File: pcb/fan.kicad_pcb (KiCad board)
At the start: 2 copper layers, 290.9 x 267.8 mm, 196 parts, among them J2 Pi, SW1 SW_PUSH, SW10 SW_PUSH, SW11 SW_PUSH, SW12 SW_PUSH, SW13 SW_PUSH, SW14 SW_PUSH, SW15 SW_PUSH, SW16 SW_PUSH, SW17 SW_PUSH, SW18 SW_PUSH, SW19 SW_PUSH, SW2 SW_PUSH, SW20 SW_PUSH, SW21 SW_PUSH, SW22 SW_PUSH, SW23 SW_PUSH, SW24 SW_PUSH, SW25 SW_PUSH, SW26 SW_PUSH, SW27 SW_PUSH, SW28 SW_PUSH, SW29 SW_PUSH, SW3 SW_PUSH, SW30 SW_PUSH, SW31 SW_PUSH, SW32 SW_PUSH, SW33 SW_PUSH, SW34 SW_PUSH, SW35 SW_PUSH, SW36 SW_PUSH, SW37 SW_PUSH, SW38 SW_PUSH, SW39 SW_PUSH, SW4 SW_PUSH, SW40 SW_PUSH, SW41 SW_PUSH, SW42 SW_PUSH, SW43 SW_PUSH, SW44 SW_PUSH, SW45 SW_PUSH, SW46 SW_PUSH, SW47 SW_PUSH, SW48 SW_PUSH, SW49 SW_PUSH, SW5 SW_PUSH, SW50 SW_PUSH, SW51 SW_PUSH, SW52 SW_PUSH, SW53 SW_PUSH, SW54 SW_PUSH, SW55 SW_PUSH, SW56 SW_PUSH, SW57 SW_PUSH, SW58 SW_PUSH, SW59 SW_PUSH, SW6 SW_PUSH, SW60 SW_PUSH, SW61 SW_PUSH, SW62 SW_PUSH, SW63 SW_PUSH, SW64 SW_PUSH, SW65 SW_PUSH, SW66 SW_PUSH, SW67 SW_PUSH, SW68 SW_PUSH, SW69 SW_PUSH, SW7 SW_PUSH, SW70 SW_PUSH, SW71 SW_PUSH, SW72 SW_PUSH, SW73 SW_PUSH, SW74 SW_PUSH, SW75 SW_PUSH, SW76 SW_PUSH, SW77 SW_PUSH, SW78 SW_PUSH, SW79 SW_PUSH, SW8 SW_PUSH, SW80 SW_PUSH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

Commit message: v2.0 外形考え中
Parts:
- removed D1, D10, D11, D12, D13, D14, D15, D16, D17, D18, D19, D2, D20, D21, D22, D23, D24, D25, D26, D27, D28, D29, D3, D30, D31, D32, D33, D34, D35, D36, D37, D38, D39, D4, D40, D41, D42, D43, D44, D45, D46, D47, D48, D49, D5, D50, D51, D52, D53, D54, D55, D56, D57, D58, D59, D6, D60, D61, D62, D63, D64, D65, D66, D67, D68, D69, D7, D70, D71, D72, D73, D74, D75, D76, D77, D78, D79, D8, D80, D81, D82, D83, D84, D85, D86, D87, D88, D89, D9, D90: DIODE, kbd:D3_TH_SMD
- removed HOLE1, HOLE2, HOLE3, HOLE4, HOLE5, HOLE6: Val**, kbd:HOLE
- removed J2: Pi, kbd:PinSocket_2x20_P2.54mm_Vertical_edit_wakunasi
- removed SW43, SW44, SW45, SW46, SW47, SW48, SW51, SW52, SW53, SW54, SW56, SW57, SW58, SW59, SW60, SW61, SW62, SW63, SW64, SW65, SW66, SW67, SW68, SW69, SW70, SW71, SW72, SW73, SW74, SW75, SW76, SW77, SW78, SW79, SW80, SW81, SW82, SW83, SW84, SW85, SW86, SW87, SW88, SW89, SW90: SW_PUSH, kbd:CherryMX_Hotswap_edit_wakunasi
- removed SW49, SW50, SW55, SW91, SW92: SW_PUSH, kbd:ResetSW_wakunasi
- removed SW93: SW_SPDT, kbd:SW_Slide_edit_wakunasi
- removed U4, U6: 74HC595, kbd:SN74HC595_DIP-16_W7.62mm_Socket_2
- added J*: MJ-4PP-9, kbd:MJ-4PP-9, F.Cu at (197.3, 19.1)
- SW1, SW11, SW12, SW13, SW14, SW16, SW17, SW18, SW19, SW2, SW20, SW21, SW22, SW23, SW24, SW25, SW26, SW27, SW28, SW29, SW3, SW30, SW31, SW32, SW33, SW34, SW35, SW36, SW37, SW38, SW39, SW4, SW40, SW6, SW7, SW8, SW9: value SW_PUSH -> SW_PUSH-kbd; footprint kbd:CherryMX_Hotswap_edit_wakunasi -> kbd:CherryMX_MidHeight_Hotswap_edit
- SW10, SW15, SW5: value SW_PUSH -> SW_PUSH-kbd; footprint kbd:CherryMX_Hotswap_edit_wakunasi -> kbd:ResetSW_with_diode
- SW41, SW42: footprint kbd:CherryMX_Hotswap_edit_wakunasi -> kbd:ResetSW
- moved SW36 130.0 mm to (159.4, 32.0), turned to 352 degrees
- moved SW6 125.4 mm to (41.3, 46.1), turned to 26 degrees
- moved SW11 108.9 mm to (60.3, 38.4)
- moved SW42 108.6 mm to (190.8, 72.9), turned to 90 degrees
- moved SW12 105.5 mm to (58.2, 59.6), turned to 22 degrees
- moved SW41 90.4 mm to (190.8, 62.6), turned to 90 degrees
- moved SW17 87.7 mm to (78.0, 53.8), turned to 13 degrees
- moved SW16 87.3 mm to (80.2, 33.4), turned to 10 degrees
- moved SW18 86.8 mm to (81.7, 72.6), turned to 13 degrees
- moved SW5 75.9 mm to (91.0, 103.0), turned to 194 degrees
- moved U2 73.3 mm to (183.2, 41.2), turned to 180 degrees
- moved U1 71.4 mm to (180.6, 40.1), turned to 0 degrees
- moved SW23 68.2 mm to (101.1, 69.0), turned to 8 degrees
- moved SW22 65.8 mm to (97.7, 50.3), turned to 8 degrees
- moved SW21 65.5 mm to (99.7, 30.3), turned to 6 degrees
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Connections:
- SW1 pad 1: (no net) -> col00
- SW1 pad 2: (no net) -> Net-(SW1-Pad2)
- SW10 pad 1: (no net) -> col01
- SW10 pad 2: (no net) -> Net-(SW10-Pad2)
- SW11 pad 1: (no net) -> col02
- SW11 pad 2: (no net) -> Net-(SW11-Pad2)
- SW12 pad 1: (no net) -> col02
- SW12 pad 2: (no net) -> Net-(SW12-Pad2)
- SW13 pad 1: (no net) -> col02
- SW13 pad 2: (no net) -> Net-(SW13-Pad2)
- SW14 pad 1: (no net) -> col02
- SW14 pad 2: (no net) -> Net-(SW14-Pad2)
- SW15 pad 1: (no net) -> col02
- SW15 pad 2: (no net) -> Net-(SW15-Pad2)
- SW16 pad 1: (no net) -> col03
- SW16 pad 2: (no net) -> Net-(SW16-Pad2)
- SW17 pad 1: (no net) -> col03
- SW17 pad 2: (no net) -> Net-(SW17-Pad2)
- SW18 pad 1: (no net) -> col03
- SW18 pad 2: (no net) -> Net-(SW18-Pad2)
- SW19 pad 1: (no net) -> col03
- SW19 pad 2: (no net) -> Net-(SW19-Pad2)
- SW2 pad 1: (no net) -> col00
- SW2 pad 2: (no net) -> Net-(SW2-Pad2)
- SW20 pad 1: (no net) -> col03
- SW20 pad 2: (no net) -> Net-(SW20-Pad2)
- SW21 pad 1: (no net) -> col04
- SW21 pad 2: (no net) -> Net-(SW21-Pad2)
- SW22 pad 1: (no net) -> col04
- SW22 pad 2: (no net) -> Net-(SW22-Pad2)
- SW23 pad 1: (no net) -> col04
- SW23 pad 2: (no net) -> Net-(SW23-Pad2)
- SW24 pad 1: (no net) -> col04
- SW24 pad 2: (no net) -> Net-(SW24-Pad2)
- SW25 pad 1: (no net) -> col04
- SW25 pad 2: (no net) -> Net-(SW25-Pad2)
- SW26 pad 1: (no net) -> col05
- SW26 pad 2: (no net) -> Net-(SW26-Pad2)
- SW27 pad 1: (no net) -> col05
- SW27 pad 2: (no net) -> Net-(SW27-Pad2)
- SW28 pad 1: (no net) -> col05
- SW28 pad 2: (no net) -> Net-(SW28-Pad2)
- SW29 pad 1: (no net) -> col05
- SW29 pad 2: (no net) -> Net-(SW29-Pad2)
- SW3 pad 1: (no net) -> col00
- SW3 pad 2: (no net) -> Net-(SW3-Pad2)
- SW30 pad 1: (no net) -> col05
- SW30 pad 2: (no net) -> Net-(SW30-Pad2)
- SW31 pad 1: (no net) -> col06
- SW31 pad 2: (no net) -> Net-(SW31-Pad2)
- SW32 pad 1: (no net) -> col06
- SW32 pad 2: (no net) -> Net-(SW32-Pad2)
- SW33 pad 1: (no net) -> col06
- SW33 pad 2: (no net) -> Net-(SW33-Pad2)
- SW34 pad 1: (no net) -> col06
- SW34 pad 2: (no net) -> Net-(SW34-Pad2)
- SW35 pad 1: (no net) -> col06
- SW35 pad 2: (no net) -> Net-(SW35-Pad2)
- SW36 pad 1: (no net) -> col07
- SW36 pad 2: (no net) -> Net-(SW36-Pad2)
- SW37 pad 1: (no net) -> col07
- SW37 pad 2: (no net) -> Net-(SW37-Pad2)
- SW38 pad 1: (no net) -> col07
- SW38 pad 2: (no net) -> Net-(SW38-Pad2)
- SW39 pad 1: (no net) -> col07
- SW39 pad 2: (no net) -> Net-(SW39-Pad2)
- SW4 pad 1: (no net) -> col00
- SW4 pad 2: (no net) -> Net-(SW4-Pad2)
- SW40 pad 1: (no net) -> col07
- SW40 pad 2: (no net) -> Net-(SW40-Pad2)
- SW41 pad 1: (no net) -> software_reset
- SW41 pad 2: (no net) -> GND
- SW42 pad 1: (no net) -> hardware_reset
- SW42 pad 2: (no net) -> GND
- SW5 pad 1: (no net) -> col00
- SW5 pad 2: (no net) -> Net-(SW5-Pad2)
- SW6 pad 1: (no net) -> col01
- SW6 pad 2: (no net) -> Net-(SW6-Pad2)
- SW7 pad 1: (no net) -> col01
- SW7 pad 2: (no net) -> Net-(SW7-Pad2)
- SW8 pad 1: (no net) -> col01
- SW8 pad 2: (no net) -> Net-(SW8-Pad2)
- SW9 pad 1: (no net) -> col01
- SW9 pad 2: (no net) -> Net-(SW9-Pad2)
- U1 pad 10: (no net) -> SCL
- U1 pad 11: (no net) -> RCK
- U1 pad 12: (no net) -> OE
- U1 pad 14: (no net) -> row04
- U1 pad 15: (no net) -> row03
- U1 pad 16: (no net) -> row02
- U1 pad 17: (no net) -> row01
- U1 pad 18: (no net) -> row00
- U1 pad 21: (no net) -> VCC
- U1 pad 22: (no net) -> hardware_reset
- U1 pad 23: (no net) -> GND
- U1 pad 3: (no net) -> GND
- U1 pad 4: (no net) -> GND
- U1 pad 7: (no net) -> software_reset
- U1 pad 8: (no net) -> SER
- U1 pad 9: (no net) -> SCK
- U2 pad 10: (no net) -> SCL
- U2 pad 11: (no net) -> RCK
- U2 pad 12: (no net) -> OE
- U2 pad 14: (no net) -> row04
- U2 pad 15: (no net) -> row03
- U2 pad 16: (no net) -> row02
- U2 pad 17: (no net) -> row01
- U2 pad 18: (no net) -> row00
- U2 pad 21: (no net) -> VCC
- U2 pad 22: (no net) -> hardware_reset
- U2 pad 23: (no net) -> GND
- U2 pad 3: (no net) -> GND
- U2 pad 4: (no net) -> GND
- U2 pad 7: (no net) -> software_reset
- U2 pad 8: (no net) -> SER
- U2 pad 9: (no net) -> SCK
- U3 pad 1: (no net) -> col01
- U3 pad 10: (no net) -> SCL
- U3 pad 11: (no net) -> SCK
- U3 pad 12: (no net) -> RCK
- U3 pad 13: (no net) -> OE
- U3 pad 14: (no net) -> SER
- U3 pad 15: (no net) -> col00
- U3 pad 16: (no net) -> VCC
- U3 pad 2: (no net) -> col02
- U3 pad 3: (no net) -> col03
- U3 pad 4: (no net) -> col04
- U3 pad 5: (no net) -> col05
- U3 pad 6: (no net) -> col06
- U3 pad 7: (no net) -> col07
- U3 pad 8: (no net) -> GND
- U5 pad 1: (no net) -> col01
- U5 pad 10: (no net) -> SCL
- U5 pad 11: (no net) -> SCK
- U5 pad 12: (no net) -> RCK
- U5 pad 13: (no net) -> OE
- U5 pad 14: (no net) -> SER
- U5 pad 15: (no net) -> col00
- U5 pad 16: (no net) -> VCC
- U5 pad 2: (no net) -> col02
- U5 pad 3: (no net) -> col03
- U5 pad 4: (no net) -> col04
- U5 pad 5: (no net) -> col05
- U5 pad 6: (no net) -> col06
- U5 pad 7: (no net) -> col07
- U5 pad 8: (no net) -> GND
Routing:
- net (no net): track 11725.6 -> 0.00 mm, vias 448 -> 0
- net col00: track 0.00 -> 384.7 mm
- net col01: track 0.00 -> 360.8 mm
- net col02: track 0.00 -> 326.7 mm, vias 0 -> 1
- net col03: track 0.00 -> 326.6 mm
- net col04: track 0.00 -> 314.3 mm, vias 0 -> 1
- net col07: track 0.00 -> 301.8 mm, vias 0 -> 1
- net col05: track 0.00 -> 297.4 mm, vias 0 -> 2
- net col06: track 0.00 -> 296.7 mm, vias 0 -> 3
- net row04: track 0.00 -> 257.3 mm
- net row03: track 0.00 -> 238.2 mm
- net row00: track 0.00 -> 219.1 mm
- net row02: track 0.00 -> 218.9 mm
- net row01: track 0.00 -> 208.6 mm
- net hardware_reset: track 0.00 -> 58.6 mm
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- added copper zone on B.Cu, net GND
- added copper zone on F.Cu, net GND
- removed copper zone on B.Cu, net (none)
- removed copper zone on F.Cu, net (none)
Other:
- board size 290.9 x 267.8 mm -> 211.6 x 146.1 mm

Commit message: 迷走中...元にもどす
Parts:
- moved U1 141.3 mm to (52.7, 100.2), turned to 39 degrees
- moved U2 140.4 mm to (55.4, 99.4), turned to 219 degrees
- moved SW42 127.8 mm to (63.1, 76.3), turned to 215 degrees
- moved SW41 125.6 mm to (66.7, 81.5), turned to 215 degrees
- moved U3 124.8 mm to (66.6, 124.1), turned to 41 degrees
- moved U5 123.6 mm to (69.6, 123.3), turned to 221 degrees
- moved SW15 57.3 mm to (167.6, 111.8)
- moved SW16 57.3 mm to (136.2, 45.6)
- moved SW19 57.3 mm to (131.6, 107.1)
- moved SW1 57.3 mm to (79.6, 68.8)
- moved SW10 57.3 mm to (157.2, 113.1)
- moved SW11 57.3 mm to (116.3, 50.6)
- moved SW12 57.3 mm to (114.2, 71.8)
- moved SW17 57.3 mm to (134.1, 66.0)
- moved SW21 57.3 mm to (155.8, 42.5)
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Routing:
- net col00: track 384.7 -> 202.3 mm
- net col01: track 360.8 -> 196.3 mm
- net col02: track 326.7 -> 199.0 mm
- net col04: track 314.3 -> 230.0 mm
- net col07: track 301.8 -> 219.8 mm
- net row04: track 257.3 -> 181.5 mm
- net col05: track 297.4 -> 224.8 mm, vias 2 -> 0
- net hardware_reset: track 58.6 -> 0.00 mm
- net row03: track 238.2 -> 181.2 mm
- net row02: track 218.9 -> 163.5 mm
- net VCC: track 54.6 -> 0.00 mm
- net SCL: track 48.5 -> 0.00 mm
- net SCK: track 48.5 -> 0.00 mm
- net SER: track 41.5 -> 0.00 mm
- net RCK: track 38.2 -> 0.00 mm
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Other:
- board size 211.6 x 146.1 mm -> 590.2 x 634.1 mm

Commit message: 基盤の外形を決定した
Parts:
- removed J*: MJ-4PP-9, kbd:MJ-4PP-9
- added J1: MJ-4PP-9, kbd:MJ-4PP-9, F.Cu at (228.4, 74.5)
- added Ref**: Val**, kbd:HOLE, F.Cu at (42.6, 68.3)
- added Ref**: Val**, kbd:HOLE, F.Cu at (198.7, 26.1)
- added Ref**: Val**, kbd:HOLE, F.Cu at (137.4, 105.4)
- added Ref**: Val**, kbd:HOLE, F.Cu at (232.1, 125.2)
- added Ref**: Val**, kbd:HOLE, F.Cu at (48.8, 115.2)
- moved U1 162.7 mm to (206.1, 46.0), turned to 0 degrees
- moved U2 161.9 mm to (208.7, 47.3), turned to 180 degrees
- moved SW41 158.7 mm to (225.4, 83.2), turned to 90 degrees
- moved SW42 155.0 mm to (218.0, 83.2), turned to 90 degrees
- moved U3 145.7 mm to (203.2, 73.3), turned to 0 degrees
- moved U5 144.8 mm to (206.0, 74.7), turned to 180 degrees
- moved SW10 33.5 mm to (126.5, 99.8)
- moved SW15 33.5 mm to (136.9, 98.5)
- moved SW16 33.5 mm to (105.5, 32.3)
- moved SW17 33.5 mm to (103.4, 52.7)
- moved SW19 33.5 mm to (100.9, 93.8)
- moved SW25 33.5 mm to (173.7, 108.1)
- moved SW26 33.5 mm to (145.1, 28.0)
- moved SW27 33.5 mm to (143.2, 47.2)
- moved SW28 33.5 mm to (146.5, 66.5)
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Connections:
- U1 pad 10: SCL -> RCK
- U1 pad 11: RCK -> OE
- U1 pad 12: OE -> SER
- U1 pad 2: (no net) -> data
- U1 pad 8: SER -> SCL
- U2 pad 10: SCL -> RCK
- U2 pad 11: RCK -> OE
- U2 pad 12: OE -> SER
- U2 pad 2: (no net) -> data
- U2 pad 8: SER -> SCL
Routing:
- net col00: track 202.3 -> 394.1 mm
- net col01: track 196.3 -> 365.6 mm
- net col02: track 199.0 -> 332.7 mm
- net col04: track 230.0 -> 321.1 mm
- net col07: track 219.8 -> 309.0 mm
- net VCC: track 0.00 -> 75.9 mm
- net row04: track 181.5 -> 250.2 mm
- net hardware_reset: track 0.00 -> 67.0 mm
- net software_reset: track 0.00 -> 64.3 mm
- net data: track 0.00 -> 62.0 mm
- net SCL: track 0.00 -> 60.3 mm
- net SCK: track 0.00 -> 54.6 mm
- net col05: track 224.8 -> 279.1 mm, vias 0 -> 1
- net col03: track 288.5 -> 341.3 mm, vias 0 -> 1
- net row03: track 181.2 -> 231.0 mm
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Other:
- board size 590.2 x 634.1 mm -> 211.3 x 140.3 mm

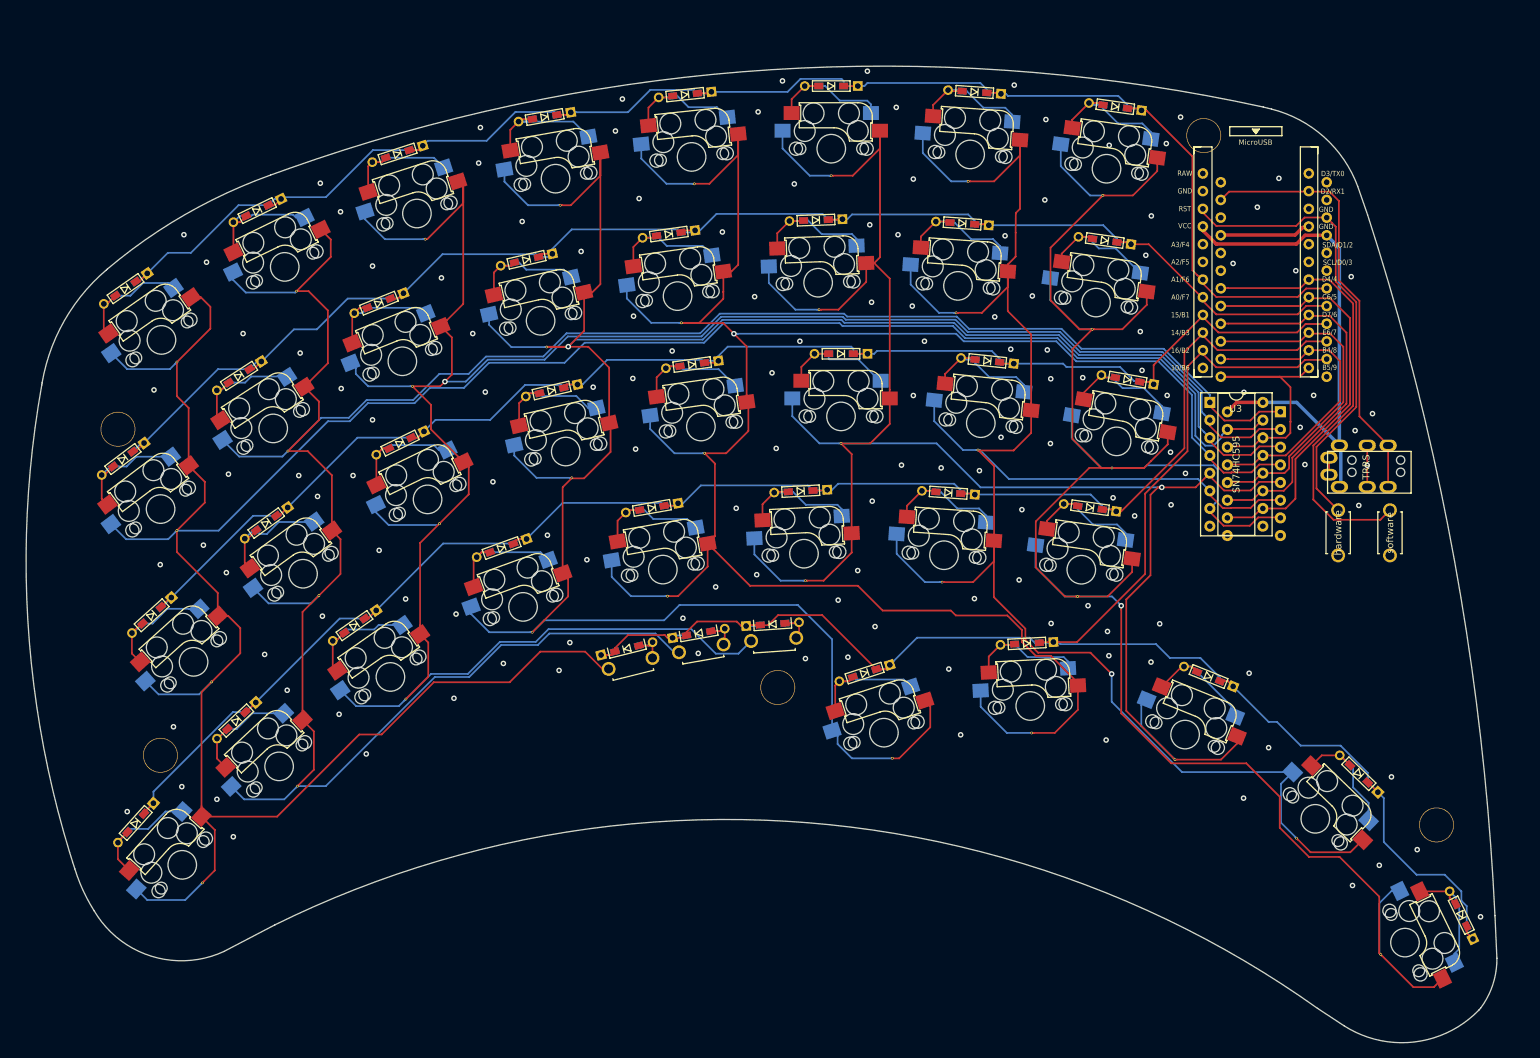
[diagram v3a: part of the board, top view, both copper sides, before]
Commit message: v2.0 fan90を受けて修正。これでpro micro用の回路は官僚とする。(ケースはまだない)
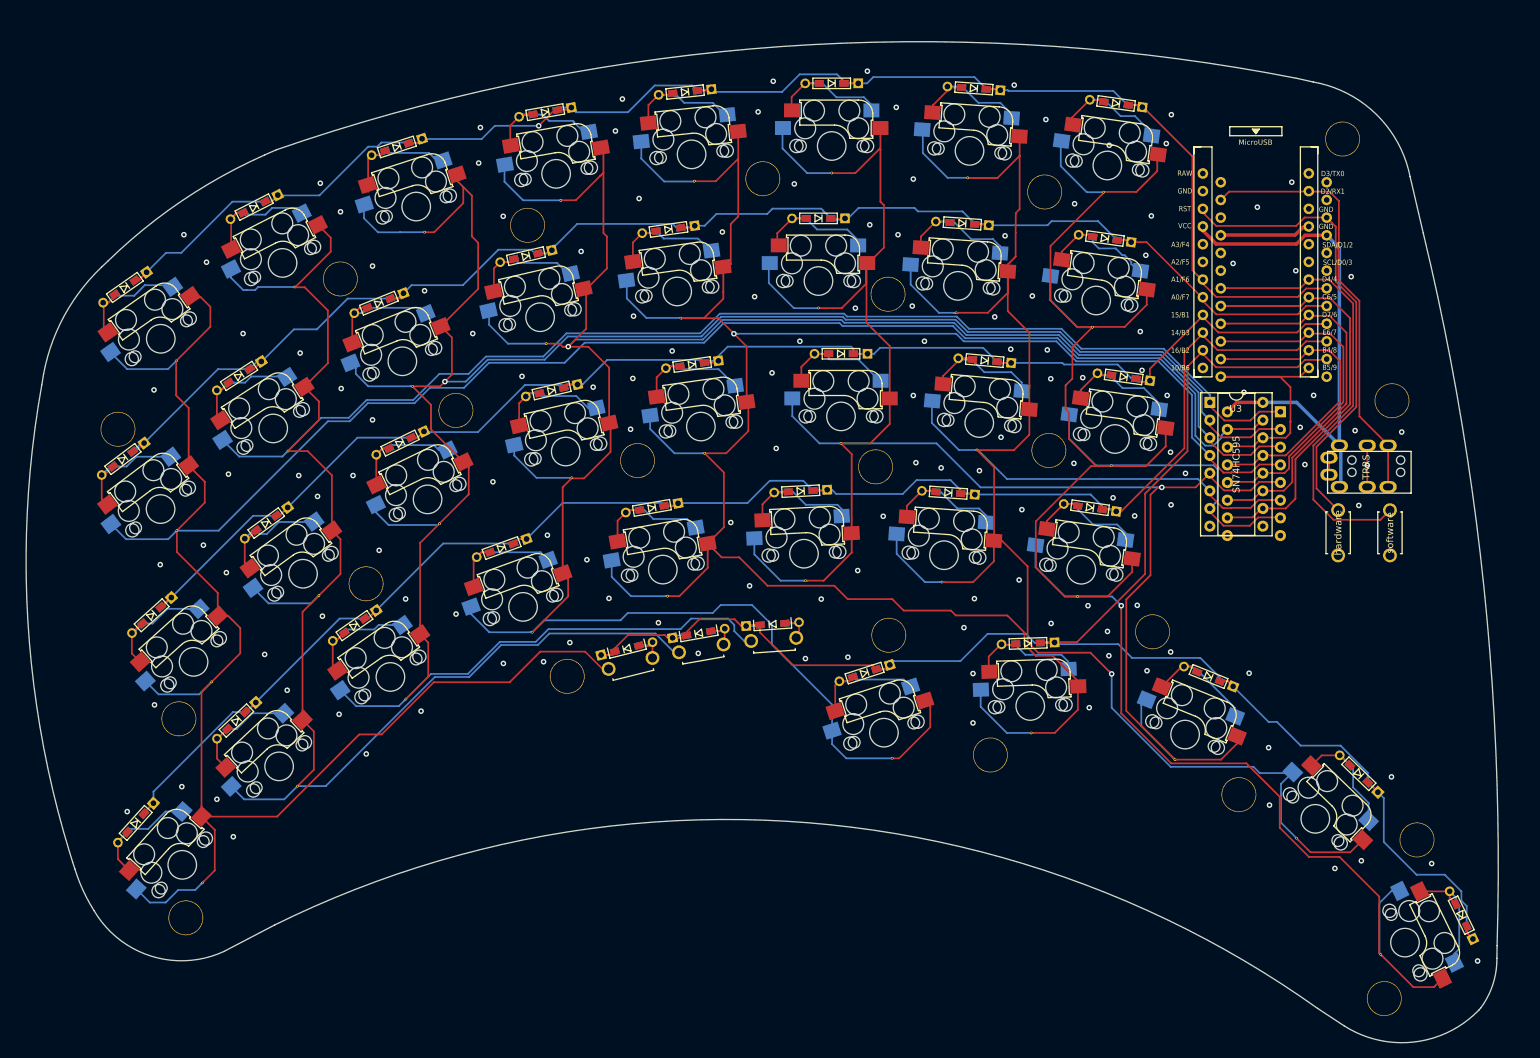
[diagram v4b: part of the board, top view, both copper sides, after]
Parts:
- removed the Ref** at (198.7, 26.1)
- removed the Ref** at (137.4, 105.4)
- removed the Ref** at (232.1, 125.2)
- added Ref**: Val**, kbd:HOLE, F.Cu at (168.0, 115.1)
- added Ref**: Val**, kbd:HOLE, F.Cu at (225.7, 64.2)
- added Ref**: Val**, kbd:HOLE, F.Cu at (203.7, 120.8)
- added Ref**: Val**, kbd:HOLE, F.Cu at (191.3, 97.4)
- added Ref**: Val**, kbd:HOLE, F.Cu at (153.4, 97.9)
- added Ref**: Val**, kbd:HOLE, F.Cu at (176.4, 71.3)
- added Ref**: Val**, kbd:HOLE, F.Cu at (135.3, 32.3)
- added Ref**: Val**, kbd:HOLE, F.Cu at (78.3, 90.5)
- added Ref**: Val**, kbd:HOLE, F.Cu at (74.6, 46.7)
- added Ref**: Val**, kbd:HOLE, F.Cu at (175.8, 34.2)
- added Ref**: Val**, kbd:HOLE, F.Cu at (218.6, 26.6)
- added Ref**: Val**, kbd:HOLE, F.Cu at (117.3, 72.8)
- added Ref**: Val**, kbd:HOLE, F.Cu at (229.3, 127.3)
- added Ref**: Val**, kbd:HOLE, F.Cu at (107.2, 103.8)
- added Ref**: Val**, kbd:HOLE, F.Cu at (153.3, 48.9)
- added Ref**: Val**, kbd:HOLE, F.Cu at (91.2, 65.6)
- added Ref**: Val**, kbd:HOLE, F.Cu at (151.5, 73.7)
- added Ref**: Val**, kbd:HOLE, F.Cu at (101.5, 39.0)
- added Ref**: Val**, kbd:HOLE, F.Cu at (224.6, 150.1)
- added Ref**: Val**, kbd:HOLE, F.Cu at (52.4, 138.5)
- moved Ref** 5.88 mm to (51.4, 109.9)
- moved SW11 1.01 mm to (85.5, 36.3)
- moved SW16 0.70 mm to (105.6, 31.6)
- moved SW22 0.67 mm to (123.0, 48.5)
- moved SW6 0.65 mm to (66.3, 44.4), turned to 27 degrees
- moved SW31 0.52 mm to (165.0, 28.3)
- moved SW17 0.52 mm to (103.3, 52.2)
- moved SW36 0.48 mm to (184.8, 30.4)
- moved SW38 0.41 mm to (185.9, 69.7), turned to 352 degrees
- moved SW26 0.39 mm to (145.2, 27.6)
- moved SW21 0.37 mm to (125.1, 28.8)
- moved SW37 0.30 mm to (183.2, 49.8)
- moved SW27 0.25 mm to (143.3, 47.0), turned to 0 degrees
- moved SW33 0.22 mm to (166.4, 67.4), turned to 355 degrees
- moved SW1 0.19 mm to (48.8, 55.3)
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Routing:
- net col03: track 341.3 -> 333.0 mm
- net col02: track 332.7 -> 336.0 mm
- net col04: track 321.1 -> 319.0 mm
- net col05: track 279.1 -> 277.2 mm
- net col07: track 309.0 -> 310.5 mm
- net row03: track 231.0 -> 232.5 mm
- net row01: track 211.8 -> 213.3 mm
- net row00: track 226.4 -> 227.4 mm, vias 0 -> 1
- net Net-(SW6-Pad2): track 17.4 -> 18.4 mm
- net col01: track 365.6 -> 366.5 mm
- net Net-(SW11-Pad2): track 17.8 -> 18.7 mm
- net Net-(SW31-Pad2): track 18.4 -> 19.3 mm
- net Net-(SW16-Pad2): track 19.9 -> 20.7 mm
- net Net-(SW17-Pad2): track 18.0 -> 18.7 mm
- net Net-(SW37-Pad2): track 18.0 -> 18.7 mm
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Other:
- board size 211.3 x 140.3 mm -> 211.5 x 143.8 mm
